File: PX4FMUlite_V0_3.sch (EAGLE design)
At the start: 152 parts, among them J2 DF13-4P-1.25V, J201 DF13C-6P-1.25V, J202 DF13C-6P-1.25V, J203 DF13C-6P-1.25V, J3 DF13C-4P-1.25V, J302 DF13C-4P-1.25V, J401 DF13C-4P-1.25V, J403 DF13C-7P-1.25V, J405 DF13C-4P-1.25V, J801 JST-ZH-3, J802 DF13C-3P-1.25V, M3_MOUNT1101 MOUNT-HOLE3.1MM, M3_MOUNT1102 MOUNT-HOLE3.1MM, M3_MOUNT1103 MOUNT-HOLE3.1MM, M3_MOUNT1104 MOUNT-HOLE3.1MM, U101 STM32F4X7VX, U2 MAX3051, U401 MAX3051, U903 74LVC2G240, X101 3.2x2.5 mm / 24 MHz / 15 ppm

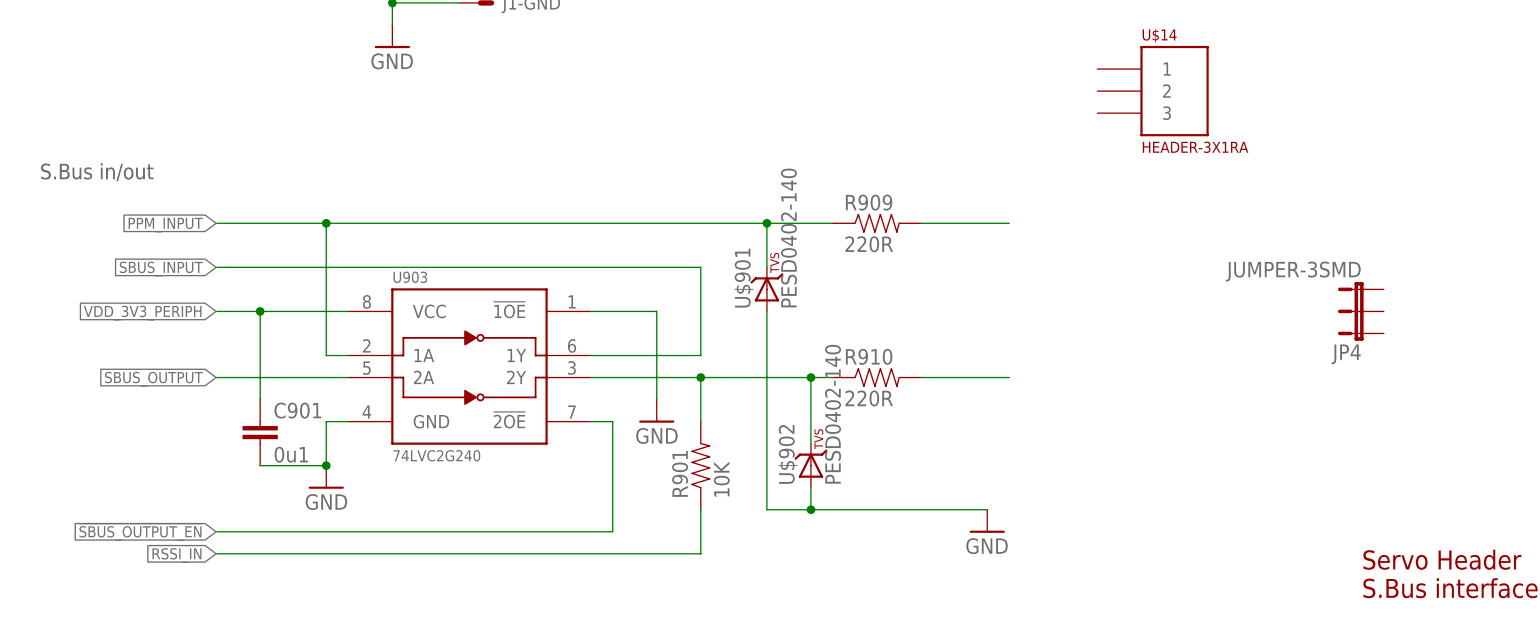
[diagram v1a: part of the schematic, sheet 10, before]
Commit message: Removed SBUS interface that would not fit
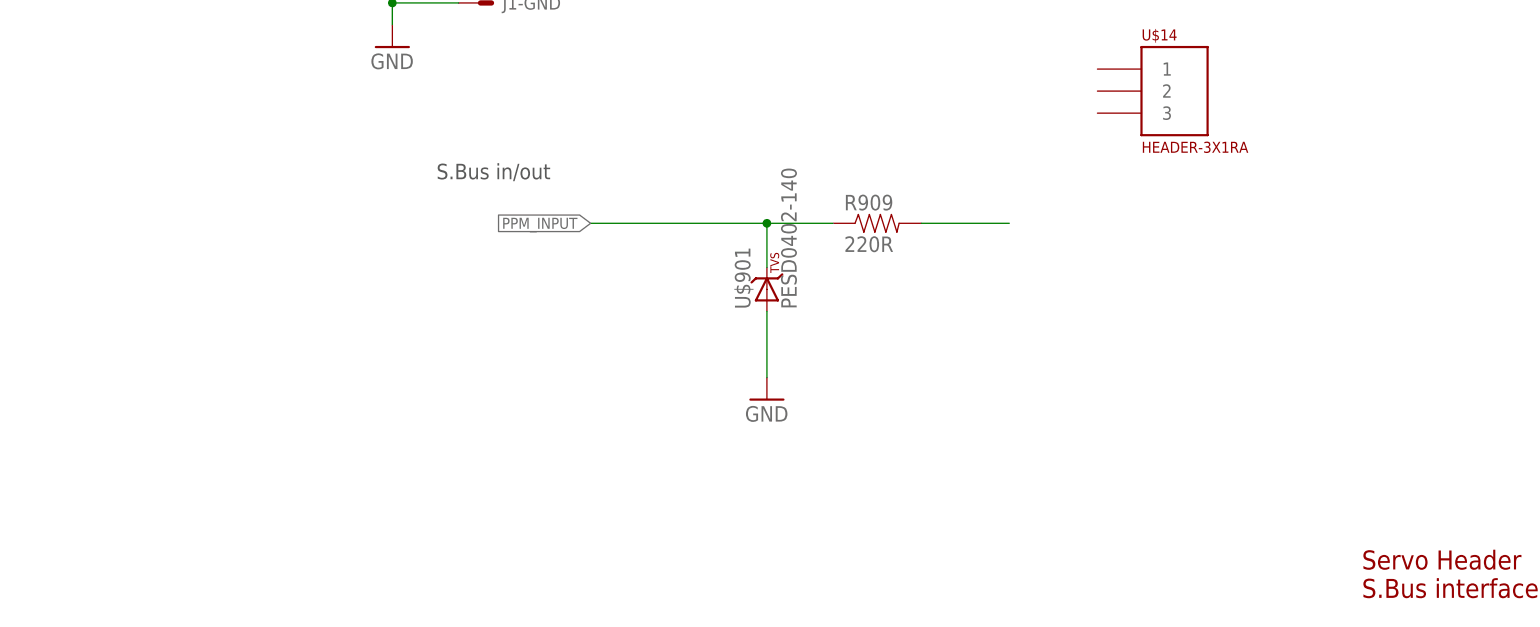
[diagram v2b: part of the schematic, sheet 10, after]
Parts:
- removed C901: 0u1, pixhawk2:CAP0402
- removed JP4: JUMPER-3SMD, SparkFun-Passives:JUMPER-3SMD
- removed R901: 10K, pixhawk2:RESISTOR0402-RES
- removed R910: 220R, pixhawk2:RESISTOR0402-RES
- removed U$902: PESD0402-140, pixhawk2:DIODE-TVS
- removed U903: 74LVC2G240, pixhawk2:74LVC2G240-TSSOP-8
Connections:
- removed net !SBUS_OUTPUT_EN: U903.!2OE
- removed net N$38: R901.2, R910.1, U$902.C, U903.2Y
- removed net N$99: R910.2
- removed net RSSI_IN: R901.1
- removed net SBUS_INPUT: U903.1Y
- removed net SBUS_OUTPUT: U903.2A
- net GND: no longer C901.2, U$902.A, U903.!1OE, U903.GND
- net PPM_INPUT: no longer U903.1A
- net VDD_3V3_PERIPH: no longer C901.1, U903.VCC
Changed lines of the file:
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@@
 </part>
 <part name="FRAME4" library="pixhawk2" deviceset="A4L-LOC" device=""/>
-<part name="GND64" library="pixhawk2" deviceset="GND" device=""/>
 <part name="FRAME8" library="pixhawk2" deviceset="A4L-LOC" device=""/>
 <part name="R713" library="pixhawk2" deviceset="RESISTOR" device="0402-RES" value="1K5">
@@
 <attribute name="PARTNO" value="RC0402FR-07470RL"/>
 </part>
-<part name="U903" library="pixhawk2" deviceset="74LVC2G240" device="-TSSOP-8" value="74LVC2G240">
-<attribute name="PARTNO" value="74LVC2G240DP,125"/>
-</part>
-<part name="R901" library="pixhawk2" deviceset="RESISTOR" device="0402-RES" value="10K">
-<attribute name="PARTNO" value="RC0402FR-0710KL"/>
-</part>
-<part name="GND51" library="pixhawk2" deviceset="GND" device=""/>
 <part name="R607" library="pixhawk2" deviceset="RESISTOR" device="0402-RES" value="10K">
 <attribute name="PARTNO" value="RC0402FR-0710KL"/>
 </part>
-<part name="C901" library="pixhawk2" deviceset="CAP" device="0402" value="0u1">
-<attribute name="PARTNO" value="CC0402ZRY5V7BB104"/>
-</part>
 <part name="L201" library="pixhawk2" deviceset="KNH16C104DA5TS" device="">
 <attribute name="PARTNO" value="KNH16C104DA5TS"/>
@@
 <attribute name="PARTNO" value="RC0402FR-07220RL"/>
 </part>
-<part name="R910" library="pixhawk2" deviceset="RESISTOR" device="0402-RES" value="220R">
-<attribute name="PARTNO" value="RC0402FR-07220RL"/>
-</part>
 <part name="FRAME10" library="pixhawk2" deviceset="A4L-LOC" device=""/>
 <part name="GND44" library="pixhawk2" deviceset="GND" device=""/>
@@
 <attribute name="PARTNO" value="PESD0402-140"/>
 </part>
-<part name="U$902" library="pixhawk2" deviceset="DIODE-TVS" device="" value="PESD0402-140">
-<attribute name="PARTNO" value="PESD0402-140"/>
-</part>
 <part name="C604" library="pixhawk2" deviceset="CAP" device="0805" value="10u/10V">
 <attribute name="PARTNO" value="CC0805ZKY5V6BB106"/>
@@
 <part name="D2" library="SparkFun-DiscreteSemi" deviceset="DIODE" device="SMA" value="B340A"/>
 <part name="D5" library="SparkFun-DiscreteSemi" deviceset="DIODE" device="SMA" value="B340A"/>
-<part name="JP4" library="SparkFun-Passives" deviceset="JUMPER-3" device="SMD"/>
 <part name="U$15" library="PX4lite" deviceset="TPS6303X" device=""/>
 <part name="U$16" library="ti_tps_soln2" deviceset="XFL4020-222MEB" device=""/>
@@
 <text x="165.1" y="15.24" size="2.1844" layer="94">Servo Header
 S.Bus interface</text>
-<text x="12.7" y="63.5" size="1.778" layer="97">S.Bus in/out</text>
+<text x="58.42" y="63.5" size="1.778" layer="97">S.Bus in/out</text>
 <text x="12.7" y="167.64" size="1.778" layer="97">Servo outputs</text>
 <text x="137.16" y="154.94" size="1.778" layer="91">1206L150/12SL littlefuse</text>
 </plain>
 <instances>
-<instance part="GND64" gate="1" x="45.72" y="27.94" rot="MR0"/>
 <instance part="FRAME8" gate="G$1" x="0" y="0"/>
-<instance part="U903" gate="G$1" x="60.96" y="40.64">
-<attribute name="PARTNO" x="60.96" y="40.64" size="1.778" layer="96" display="off"/>
-</instance>
-<instance part="R901" gate="G$1" x="88.9" y="30.48" rot="R90">
-<attribute name="PARTNO" x="88.9" y="30.48" size="1.778" layer="96" rot="R90" display="off"/>
-</instance>
-<instance part="GND51" gate="1" x="83.82" y="35.56" rot="MR0"/>
-<instance part="C901" gate="G$1" x="38.1" y="33.02">
-<attribute name="PARTNO" x="38.1" y="33.02" size="1.778" layer="96" display="off"/>
-</instance>
 <instance part="R909" gate="G$1" x="109.22" y="58.42">
 <attribute name="PARTNO" x="109.22" y="58.42" size="1.778" layer="96" display="off"/>
 </instance>
-<instance part="R910" gate="G$1" x="109.22" y="40.64">
-<attribute name="PARTNO" x="109.22" y="40.64" size="1.778" layer="96" display="off"/>
-</instance>
-<instance part="GND44" gate="1" x="121.92" y="22.86"/>
+<instance part="GND44" gate="1" x="96.52" y="38.1"/>
 <instance part="U$901" gate="G$1" x="96.52" y="50.8" rot="R90">
 <attribute name="PARTNO" x="96.52" y="50.8" size="1.778" layer="96" display="off"/>
 </instance>
-<instance part="U$902" gate="G$1" x="101.6" y="30.48" rot="R90">
-<attribute name="PARTNO" x="101.6" y="30.48" size="1.778" layer="96" display="off"/>
-</instance>
 <instance part="L1" gate="G$1" x="81.28" y="99.06"/>
 <instance part="L1" gate="G$2" x="68.58" y="104.14"/>
@@
 <instance part="J1" gate="-VCC" x="66.04" y="152.4"/>
 <instance part="U$14" gate="G$1" x="142.24" y="71.12"/>
-<instance part="JP4" gate="G$1" x="165.1" y="45.72" rot="R90"/>
 <instance part="J1" gate="-CH1" x="101.6" y="99.06"/>
 <instance part="J1" gate="-CH2" x="101.6" y="104.14"/>
@@
 <net name="PPM_INPUT" class="0">
 <segment>
-<wire x1="48.26" y1="43.18" x2="45.72" y2="43.18" width="0.1524" layer="91"/>
-<wire x1="45.72" y1="43.18" x2="45.72" y2="58.42" width="0.1524" layer="91"/>
-<wire x1="45.72" y1="58.42" x2="33.02" y2="58.42" width="0.1524" layer="91"/>
-<label x="33.02" y="58.42" size="1.27" layer="95" rot="R180" xref="yes"/>
-<pinref part="U903" gate="G$1" pin="1A"/>
+<label x="76.2" y="58.42" size="1.27" layer="95" rot="R180" xref="yes"/>
 <pinref part="R909" gate="G$1" pin="1"/>
-<wire x1="45.72" y1="58.42" x2="96.52" y2="58.42" width="0.1524" layer="91"/>
-<junction x="45.72" y="58.42"/>
+<wire x1="76.2" y1="58.42" x2="96.52" y2="58.42" width="0.1524" layer="91"/>
 <pinref part="U$901" gate="G$1" pin="C"/>
 <wire x1="96.52" y1="58.42" x2="104.14" y2="58.42" width="0.1524" layer="91"/>
@@
 </segment>
 </net>
-<net name="SBUS_INPUT" class="0">
-<segment>
-<wire x1="76.2" y1="43.18" x2="88.9" y2="43.18" width="0.1524" layer="91"/>
-<wire x1="88.9" y1="43.18" x2="88.9" y2="53.34" width="0.1524" layer="91"/>
-<wire x1="88.9" y1="53.34" x2="33.02" y2="53.34" width="0.1524" layer="91"/>
-<label x="33.02" y="53.34" size="1.27" layer="95" rot="R180" xref="yes"/>
-<pinref part="U903" gate="G$1" pin="1Y"/>
-</segment>
-</net>
-<net name="SBUS_OUTPUT" class="0">
-<segment>
-<wire x1="48.26" y1="40.64" x2="33.02" y2="40.64" width="0.1524" layer="91"/>
-<label x="33.02" y="40.64" size="1.27" layer="95" rot="R180" xref="yes"/>
-<pinref part="U903" gate="G$1" pin="2A"/>
-</segment>
-</net>
-<net name="N$38" class="0">
-<segment>
-<wire x1="76.2" y1="40.64" x2="88.9" y2="40.64" width="0.1524" layer="91"/>
-<pinref part="U903" gate="G$1" pin="2Y"/>
-<pinref part="R901" gate="G$1" pin="2"/>
-<wire x1="88.9" y1="40.64" x2="88.9" y2="35.56" width="0.1524" layer="91"/>
-<pinref part="R910" gate="G$1" pin="1"/>
-<wire x1="88.9" y1="40.64" x2="101.6" y2="40.64" width="0.1524" layer="91"/>
-<junction x="88.9" y="40.64"/>
-<pinref part="U$902" gate="G$1" pin="C"/>
-<wire x1="101.6" y1="40.64" x2="104.14" y2="40.64" width="0.1524" layer="91"/>
-<wire x1="101.6" y1="33.02" x2="101.6" y2="40.64" width="0.1524" layer="91"/>
-<junction x="101.6" y="40.64"/>
-</segment>
-</net>
-<net name="RSSI_IN" class="0">
-<segment>
-<pinref part="R901" gate="G$1" pin="1"/>
-<wire x1="88.9" y1="25.4" x2="88.9" y2="20.32" width="0.1524" layer="91"/>
-<wire x1="88.9" y1="20.32" x2="33.02" y2="20.32" width="0.1524" layer="91"/>
-<label x="33.02" y="20.32" size="1.27" layer="95" rot="R180" xref="yes"/>
-</segment>
-</net>
-<net name="!SBUS_OUTPUT_EN" class="0">
-<segment>
-<pinref part="U903" gate="G$1" pin="!2OE"/>
-<wire x1="76.2" y1="35.56" x2="78.74" y2="35.56" width="0.1524" layer="91"/>
-<wire x1="78.74" y1="35.56" x2="78.74" y2="22.86" width="0.1524" layer="91"/>
-<wire x1="78.74" y1="22.86" x2="33.02" y2="22.86" width="0.1524" layer="91"/>
-<label x="33.02" y="22.86" size="1.27" layer="95" rot="R180" xref="yes"/>
-</segment>
-</net>
 <net name="N$68" class="0">
 <segment>
@@
 </segment>
 </net>
-<net name="N$99" class="0">
-<segment>
-<pinref part="R910" gate="G$1" pin="2"/>
-<wire x1="114.3" y1="40.64" x2="124.46" y2="40.64" width="0.1524" layer="91"/>
-</segment>
-</net>
 <net name="V_SERVO" class="1">
 <segment>
@@
 </segment>
 <segment>
-<wire x1="48.26" y1="35.56" x2="45.72" y2="35.56" width="0.1524" layer="91"/>
-<wire x1="45.72" y1="35.56" x2="45.72" y2="30.48" width="0.1524" layer="91"/>
-<pinref part="GND64" gate="1" pin="GND"/>
-<pinref part="U903" gate="G$1" pin="GND"/>
-<pinref part="C901" gate="G$1" pin="2"/>
-<wire x1="45.72" y1="30.48" x2="38.1" y2="30.48" width="0.1524" layer="91"/>
-<junction x="45.72" y="30.48"/>
-</segment>
-<segment>
-<pinref part="U903" gate="G$1" pin="!1OE"/>
-<wire x1="76.2" y1="48.26" x2="83.82" y2="48.26" width="0.1524" layer="91"/>
-<wire x1="83.82" y1="48.26" x2="83.82" y2="38.1" width="0.1524" layer="91"/>
-<pinref part="GND51" gate="1" pin="GND"/>
-</segment>
-<segment>
 <pinref part="GND44" gate="1" pin="GND"/>
 <pinref part="U$901" gate="G$1" pin="A"/>
-<wire x1="96.52" y1="48.26" x2="96.52" y2="25.4" width="0.1524" layer="91"/>
-<wire x1="96.52" y1="25.4" x2="101.6" y2="25.4" width="0.1524" layer="91"/>
-<pinref part="U$902" gate="G$1" pin="A"/>
-<wire x1="101.6" y1="25.4" x2="121.92" y2="25.4" width="0.1524" layer="91"/>
-<wire x1="101.6" y1="27.94" x2="101.6" y2="25.4" width="0.1524" layer="91"/>
-<junction x="101.6" y="25.4"/>
+<wire x1="96.52" y1="48.26" x2="96.52" y2="40.64" width="0.1524" layer="91"/>
 </segment>
 </net>
@@
 </segment>
 </net>
-<net name="VDD_3V3_PERIPH" class="1">
-<segment>
-<wire x1="48.26" y1="48.26" x2="38.1" y2="48.26" width="0.1524" layer="91"/>
-<label x="33.02" y="48.26" size="1.27" layer="95" rot="MR0" xref="yes"/>
-<pinref part="U903" gate="G$1" pin="VCC"/>
-<pinref part="C901" gate="G$1" pin="1"/>
-<wire x1="38.1" y1="48.26" x2="33.02" y2="48.26" width="0.1524" layer="91"/>
-<wire x1="38.1" y1="38.1" x2="38.1" y2="48.26" width="0.1524" layer="91"/>
-<junction x="38.1" y="48.26"/>
-</segment>
-</net>

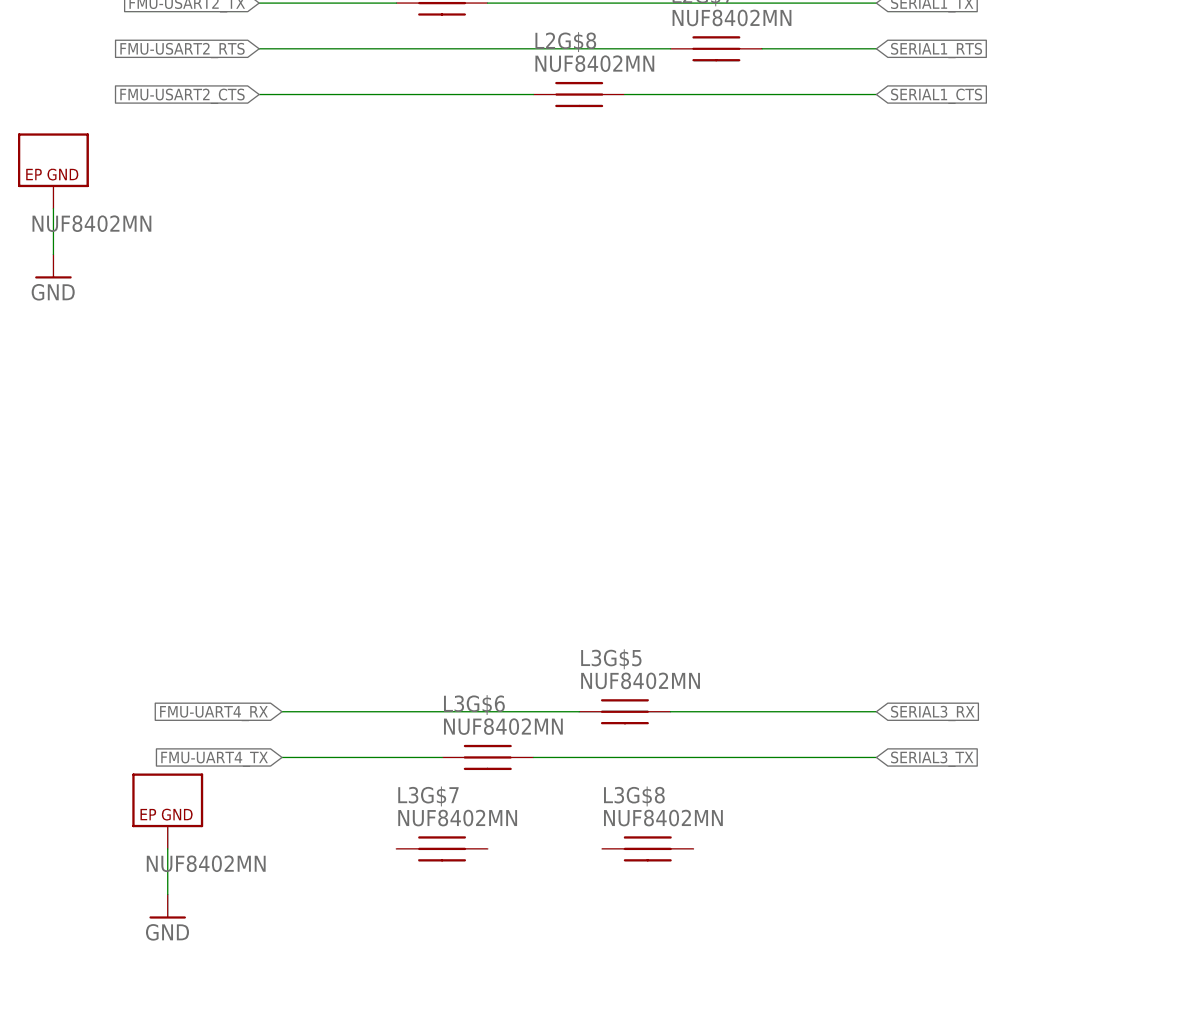
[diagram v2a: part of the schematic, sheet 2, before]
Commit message: Reworked PPM and spektrum through ESD/filter
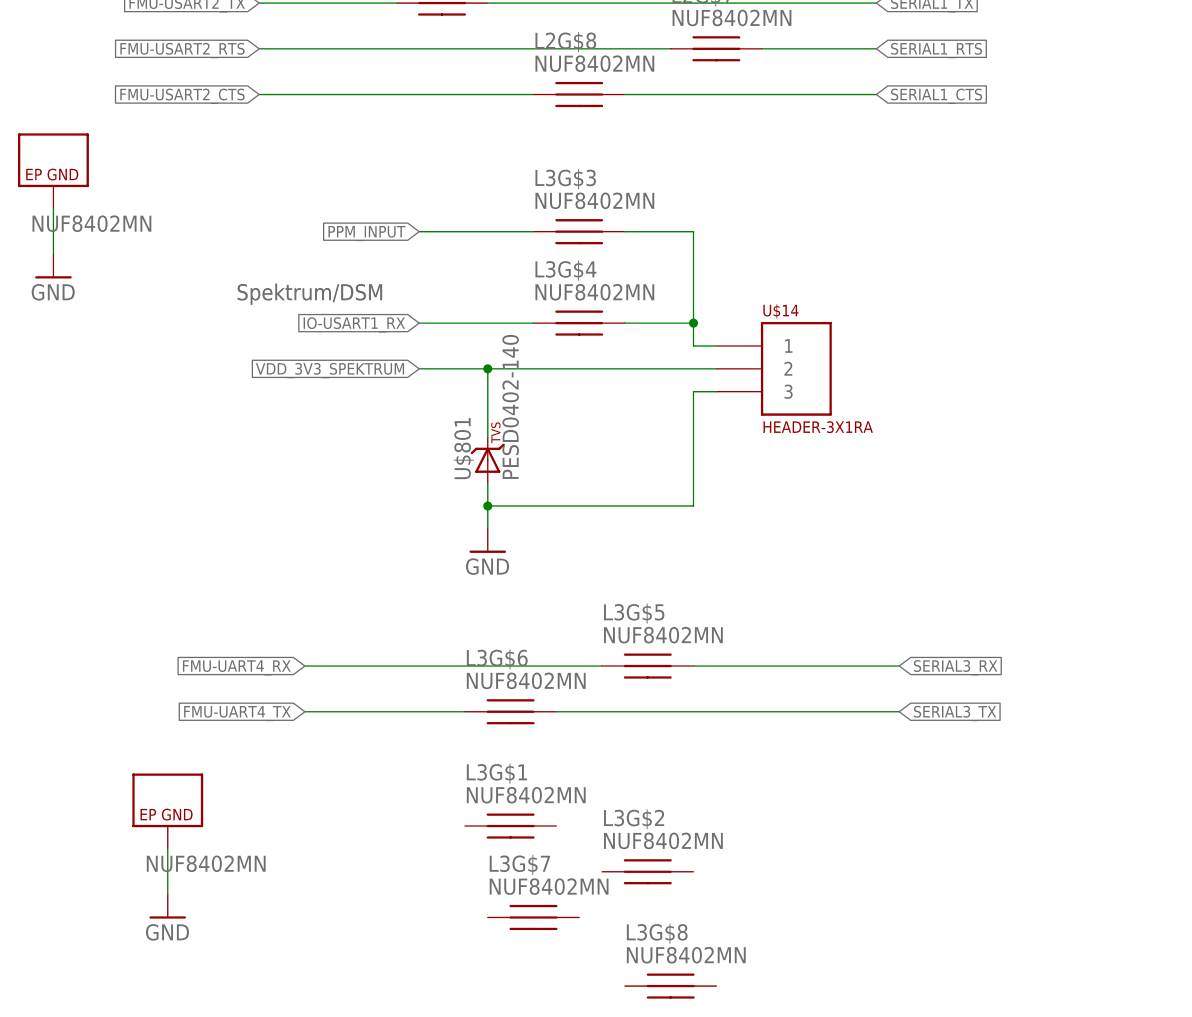
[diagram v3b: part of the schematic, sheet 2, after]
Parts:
- removed J801: JST-ZH-3, for-transfers:JST-ZH-3
- removed R909: 220R, pixhawk2:RESISTOR0402-RES
- removed U$901: PESD0402-140, pixhawk2:DIODE-TVS
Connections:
- removed net PPM-SBUS-PROT: R909.2
- removed net PPM_INPUT: R909.1, U$901.C
- new net N$18: L3G$3.P$2, L3G$4.P$2, U$14.1
- net GND: now also U$14.3; no longer J801.P$2, U$901.A
- net IO-USART1_RX: now also L3G$4.P$1; no longer J801.P$3
- net VDD_3V3_SPEKTRUM: now also U$14.2; no longer J801.P$1
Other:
- note removed: "S.Bus in/out"
- moved on the sheet: L3G$5, L3G$6, L3G$7, L3G$8
